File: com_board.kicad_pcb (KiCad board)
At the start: 2 copper layers, 25 parts, among them J1 USB_C_Receptacle_USB2.0_16P, J2 Conn_ST_STDC14, U1 nRF52820-QDxx, Y1 32.768kHz Cl=9pF, Y2 32MHz Cl=8pF

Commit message: Fixed libs
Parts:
- added C16: 820pF, Capacitor_SMD:C_0201_0603Metric, F.Cu at (170.0, 113.4)
- added C17: 1uF, Capacitor_SMD:C_0402_1005Metric_Pad0.74x0.62mm_HandSolder, F.Cu at (181.1, 91.5)
- added C18: 1uF, Capacitor_SMD:C_0402_1005Metric_Pad0.74x0.62mm_HandSolder, F.Cu at (181.1, 93.5)
- added H1: MountingHole, MountingHole:MountingHole_2.2mm_M2, F.Cu at (166.9, 78.2)
- added H2: MountingHole, MountingHole:MountingHole_2.2mm_M2, F.Cu at (166.9, 84.2)
- added H3: MountingHole, MountingHole:MountingHole_2.2mm_M2, F.Cu at (166.9, 90.2)
- added H4: MountingHole, MountingHole:MountingHole_2.2mm_M2, F.Cu at (166.9, 96.1)
- added IC1: nRF52820-QDAA-R, NRF52qdaa:QFN40P500X500X90-41N-D, F.Cu at (158.8, 108.0)
- added JP1: SolderJumper_3_Open, Jumper:SolderJumper-3_P1.3mm_Open_Pad1.0x1.5mm_NumberLabels, F.Cu at (158.0, 113.3)
- added POW_5V1: FFC-FPC:TE_84952_4, Connector_FFC-FPC:TE_84952-4_1x04-1MP_P1.0mm_Horizontal, F.Cu at (206.1, 93.8)
- added R1: 5.1K, Resistor_SMD:R_0402_1005Metric_Pad0.72x0.64mm_HandSolder, F.Cu at (177.2, 110.1)
- added R2: 5.1K, Resistor_SMD:R_0402_1005Metric_Pad0.72x0.64mm_HandSolder, F.Cu at (177.2, 112.0)
- added R3: 5.1K, Resistor_SMD:R_0402_1005Metric_Pad0.72x0.64mm_HandSolder, F.Cu at (177.2, 114.0)
- added TP10: TestPoint, TestPoint:TestPoint_Pad_D1.0mm, F.Cu at (150.6, 105.8)
- added TP11: TestPoint, TestPoint:TestPoint_Pad_D1.0mm, F.Cu at (150.6, 108.9)
- added TP12: TestPoint, TestPoint:TestPoint_Pad_D1.0mm, F.Cu at (150.6, 112.0)
- added TP13: TestPoint, TestPoint:TestPoint_Pad_D1.0mm, F.Cu at (153.6, 105.8)
- added TP14: TestPoint, TestPoint:TestPoint_Pad_D1.0mm, F.Cu at (153.6, 108.9)
- added TP15: TestPoint, TestPoint:TestPoint_Pad_D1.0mm, F.Cu at (153.6, 112.0)
- added TP4: TestPoint, TestPoint:TestPoint_Pad_D1.0mm, F.Cu at (144.5, 105.8)
- added TP5: TestPoint, TestPoint:TestPoint_Pad_D1.0mm, F.Cu at (144.5, 108.9)
- added TP6: TestPoint, TestPoint:TestPoint_Pad_D1.0mm, F.Cu at (144.5, 112.0)
- added TP7: TestPoint, TestPoint:TestPoint_Pad_D1.0mm, F.Cu at (147.5, 105.8)
- added TP8: TestPoint, TestPoint:TestPoint_Pad_D1.0mm, F.Cu at (147.5, 108.9)
- added TP9: TestPoint, TestPoint:TestPoint_Pad_D1.0mm, F.Cu at (147.5, 112.0)
- added U2: USBLC6-2SC6, Package_TO_SOT_SMD:SOT-23-6, F.Cu at (180.9, 101.5)
- added U5: AP2112K-3.3, Package_TO_SOT_SMD:SOT-23-5, F.Cu at (180.9, 106.1)
- U1: value nRF52820-QDxx -> BU-01; footprint Package_DFN_QFN:QFN-40-1EP_5x5mm_P0.4mm_EP3.6x3.6mm -> bu-01:BU-01
- moved J1 73.9 mm to (119.7, 117.3)
- moved C12 37.4 mm to (181.1, 89.6)
- moved C8 37.4 mm to (181.1, 87.6)
- moved TP2 30.8 mm to (141.4, 108.9)
- moved TP1 30.8 mm to (141.4, 105.8)
- moved TP3 30.8 mm to (141.4, 112.0)
- moved Y2 29.6 mm to (180.8, 110.9)
- moved Y1 28.7 mm to (181.1, 114.1)
- moved C10 25.0 mm to (173.4, 112.8)
- moved C13 25.0 mm to (173.4, 115.3)
- moved C9 25.0 mm to (173.4, 110.3)
- moved U1 21.7 mm to (145.4, 90.8)
- moved C11 21.4 mm to (167.6, 115.2)
- moved C6 21.4 mm to (167.6, 111.7)
- moved C7 21.4 mm to (167.6, 113.4)
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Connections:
- C1 pad 1: Net-(U1-XL1/P0.00) -> Net-(IC1-P0.00)
- C11 pad 1: Net-(U1-DEC3) -> Net-(IC1-DEC3)
- C12 pad 1: Net-(U1-DEC4) -> Net-(IC1-DEC4)
- C13 pad 1: Net-(U1-DECUSB) -> Net-(IC1-DECUSB)
- C14 pad 1: Net-(U1-ANT) -> Net-(IC1-ANT)
- C2 pad 1: Net-(U1-XL2/P0.01) -> Net-(IC1-P0.01)
- C3 pad 1: Net-(U1-XC1) -> Net-(IC1-XC2)
- C4 pad 1: Net-(U1-XC2) -> Net-(IC1-XC1)
- C5 pad 1: VDD_NRF -> 3.3V_VDD
- C6 pad 1: VDD_NRF -> 3.3V_VDD
- C7 pad 1: Net-(U1-DEC1) -> Net-(IC1-DEC1)
- C8 pad 1: VDD_NRF -> 3.3V_VDD
- C9 pad 1: VDD_NRF -> 3.3V_VDD
- J1 pad A1: Net-(J1-GND-PadA1) -> GND
- J1 pad A12: Net-(J1-GND-PadA1) -> GND
- J1 pad A4: Net-(J1-VBUS-PadA4) -> VBUS
- J1 pad A5: unconnected-(J1-CC1-PadA5) -> Net-(J1-CC1)
- J1 pad A6: unconnected-(J1-D+-PadA6) -> Net-(J1-D+-PadA6)
- J1 pad A7: unconnected-(J1-D--PadA7) -> Net-(J1-D--PadA7)
- J1 pad A9: Net-(J1-VBUS-PadA4) -> VBUS
- J1 pad B1: Net-(J1-GND-PadA1) -> GND
- J1 pad B12: Net-(J1-GND-PadA1) -> GND
- J1 pad B4: Net-(J1-VBUS-PadA4) -> VBUS
- J1 pad B5: unconnected-(J1-CC2-PadB5) -> Net-(J1-CC2)
- J1 pad B6: unconnected-(J1-D+-PadB6) -> Net-(J1-D+-PadA6)
- J1 pad B7: unconnected-(J1-D--PadB7) -> Net-(J1-D--PadA7)
- J1 pad B9: Net-(J1-VBUS-PadA4) -> VBUS
- J1 pad S1: unconnected-(J1-SHIELD-PadS1) -> GND
- J2 pad 3: VDD_NRF -> 3.3V_VDD
- L1 pad 1: Net-(U1-ANT) -> Net-(IC1-ANT)
- L2 pad 2: unconnected-(L2-Pad2) -> Net-(J3-SIG)
- U1 pad 1: Net-(U1-DEC1) -> unconnected-(U1-EXTON-Pad1)
- U1 pad 10: VBUS -> unconnected-(U1-GPIO5-Pad10)
- U1 pad 11: Net-(U1-DECUSB) -> unconnected-(U1-GPIO4-Pad11)
- U1 pad 16: /nRST -> GND
- U1 pad 17: unconnected-(U1-P0.20-Pad17) -> /SPI_CS
- U1 pad 18: VDD_NRF -> /SPI_MOSI
- U1 pad 19: /SWDIO -> /SPI_MISO
- U1 pad 2: Net-(U1-XL1/P0.00) -> unconnected-(U1-WAKEUP-Pad2)
- U1 pad 20: /SWDCLK -> /SPI_CLK
- U1 pad 21: unconnected-(U1-DEC5-Pad21) -> GND
- U1 pad 22: unconnected-(U1-P0.16-Pad22) -> /BU-01_IRQ
- U1 pad 23: unconnected-(U1-P0.17-Pad23) -> GND
- U1 pad 24: Net-(U1-ANT) -> GND
- U1 pad 3: Net-(U1-XL2/P0.01) -> /BU-01_RSTn
- U1 pad 5: unconnected-(U1-AIN3/P0.05-Pad5) -> 3.3V_VDD
- U1 pad 6: unconnected-(U1-P0.06-Pad6) -> 3.3V_VDD
- U1 pad 7: unconnected-(U1-P0.07-Pad7) -> 3.3V_VDD
- U1 pad 8: VDD_NRF -> GND
- U1 pad 9: VDD_NRF -> unconnected-(U1-GPIO6-Pad9)
- Y1 pad 1: Net-(U1-XL2/P0.01) -> Net-(IC1-P0.01)
- Y1 pad 2: Net-(U1-XL1/P0.00) -> Net-(IC1-P0.00)
- Y2 pad 1: Net-(U1-XC2) -> Net-(IC1-XC1)
- Y2 pad 3: Net-(U1-XC1) -> Net-(IC1-XC2)

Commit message: Almost done
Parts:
- added J3: U.FL-R-SMT_01_, UFL:HRS_U.FL-R-SMT_01_, F.Cu at (129.2, 116.1)
- moved R3 79.1 mm to (100.3, 96.0)
- moved H2 75.8 mm to (100.0, 120.0)
- moved H4 67.1 mm to (100.0, 90.0)
- moved POW_5V1 60.1 mm to (147.0, 105.0), turned to 90 degrees
- moved TP13 55.2 mm to (99.7, 94.0)
- moved C8 54.6 mm to (127.9, 99.9), turned to 90 degrees
- moved Y1 52.4 mm to (131.0, 98.9)
- moved U1 52.3 mm to (97.1, 111.0), turned to 90 degrees
- moved TP12 50.6 mm to (100.0, 113.5)
- moved C13 50.5 mm to (124.2, 104.4), turned to 180 degrees
- moved C10 50.4 mm to (124.1, 102.7), turned to 180 degrees
- moved J2 49.4 mm to (125.3, 90.5), turned to -90 degrees
- moved TP10 49.0 mm to (102.7, 95.5)
- moved C12 48.8 mm to (134.8, 105.0)
- moved C9 48.4 mm to (126.2, 99.6), turned to 90 degrees
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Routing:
- net 3.3V_VDD: track 0.00 -> 10.5 mm
- net Net-(J1-D--PadA7): track 0.00 -> 5.66 mm
- net Net-(IC1-XC1): track 0.00 -> 5.31 mm
- net GND: track 0.00 -> 5.23 mm
- net Net-(J1-D+-PadA6): track 0.00 -> 4.89 mm
- net Net-(IC1-XC2): track 0.00 -> 4.86 mm
- net Net-(IC1-P0.01): track 0.00 -> 4.41 mm
- net Net-(IC1-P0.00): track 0.00 -> 4.33 mm
- net Net-(J1-CC1): track 0.00 -> 3.34 mm
- net VBUS: track 0.00 -> 3.26 mm
- net Net-(J1-CC2): track 0.00 -> 3.21 mm
- net Net-(IC1-DECUSB): track 0.00 -> 2.75 mm
- net Net-(IC1-ANT): track 0.00 -> 2.60 mm
- net Net-(IC1-DEC1): track 0.00 -> 2.51 mm
- net Net-(J3-SIG): track 0.00 -> 2.29 mm
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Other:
- board outline added: 58 x 38 mm

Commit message: Worked on layou
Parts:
- moved C18 0.87 mm to (143.0, 115.3), turned to 0 degrees
- moved TP2 0.58 mm to (126.6, 95.9)
- moved TP6 0.43 mm to (141.6, 105.5)
- moved TP7 0.43 mm to (141.6, 103.3)
- moved C8 0.31 mm to (127.6, 100.0)
- moved TP3 0.24 mm to (129.2, 95.9)
- moved TP1 0.23 mm to (122.8, 95.9)
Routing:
- net GND: track 5.23 -> 28.9 mm, vias 0 -> 22
- net /UART_RX: track 0.00 -> 13.1 mm
- net /UART_TX: track 0.00 -> 6.58 mm, vias 0 -> 2
- net /BU-01_IRQ: track 0.00 -> 5.95 mm
- net /SPI_CS: track 0.00 -> 5.60 mm
- net 3.3V_VDD: track 10.5 -> 6.91 mm
- net Net-(J1-D+-PadA6): track 4.89 -> 6.96 mm
- net /BU-01_RSTn: track 0.00 -> 1.71 mm, vias 0 -> 1
- added copper zone on In1.Cu, net GND
- added copper zone on In2.Cu, net GND
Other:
- copper layers 2 -> 4

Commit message: first iteration
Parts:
- removed POW_5V1: FFC-FPC:TE_84952_4, Connector_FFC-FPC:TE_84952-4_1x04-1MP_P1.0mm_Horizontal
- removed TP14, TP15: TestPoint, TestPoint:TestPoint_Pad_D1.0mm
- added TP16: TestPoint, TestPoint:TestPoint_Pad_D1.0mm, F.Cu at (137.4, 108.3)
- added TP17: TestPoint, TestPoint:TestPoint_Pad_D1.0mm, F.Cu at (138.4, 105.9)
- added UART_conn1: FFC-FPC:TE_84952_6, Connector_FFC-FPC:TE_84952-6_1x06-1MP_P1.0mm_Horizontal, F.Cu at (147.0, 104.7)
- moved C9 9.10 mm to (121.5, 107.5), turned to 180 degrees
- moved C10 3.31 mm to (126.0, 100.0), turned to 90 degrees
- moved J3 1.84 mm to (128.4, 117.7)
- moved C15 1.84 mm to (127.2, 112.0)
- moved C14 1.84 mm to (127.2, 111.2)
- moved L1 1.84 mm to (128.5, 111.6)
- moved L2 1.84 mm to (128.5, 113.5)
- moved C13 1.34 mm to (124.1, 103.1)
- moved C12 0.81 mm to (135.6, 104.9)
- moved TP6 0.76 mm to (141.7, 104.8)
- moved TP7 0.57 mm to (141.7, 102.7)
- moved TP4 0.44 mm to (141.0, 120.2)
- moved C16 0.39 mm to (125.8, 108.3)
- moved C8 0.28 mm to (127.6, 99.7)
- moved TP2 0.27 mm to (126.4, 95.7)
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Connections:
- IC1 pad 33: unconnected-(IC1-P0.30-Pad33) -> /INT
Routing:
- net /BU-01_RSTn: track 1.71 -> 42.7 mm, vias 1 -> 2
- net 3.3V_VDD: track 6.91 -> 47.3 mm, vias 0 -> 43
- net /BU-01_IRQ: track 5.95 -> 45.3 mm, vias 0 -> 2
- net /SWDCLK: track 0.00 -> 33.9 mm, vias 0 -> 2
- net /SPI_CLK: track 0.00 -> 32.9 mm, vias 0 -> 2
- net /SWDIO: track 0.00 -> 31.9 mm, vias 0 -> 2
- net /SPI_MISO: track 0.00 -> 31.2 mm, vias 0 -> 2
- net VBUS: track 3.26 -> 33.3 mm, vias 0 -> 5
- net /SPI_MOSI: track 0.00 -> 28.6 mm, vias 0 -> 2
- net /SPI_CS: track 5.60 -> 31.6 mm, vias 0 -> 2
- net GND: track 28.9 -> 53.9 mm, vias 22 -> 273
- net /nRST: track 0.00 -> 23.8 mm
- net /UBS_D-: track 0.00 -> 22.5 mm, vias 0 -> 2
- net /UBS_D+: track 0.00 -> 22.3 mm, vias 0 -> 2
- net /POWER_EN: track 0.00 -> 16.1 mm
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- added copper zone on B.Cu, net 3.3V_VDD
- added copper zone on F.Cu, net 3.3V_VDD
- added copper zone on F.Cu, net GND
- added copper zone on B.Cu, net VBUS

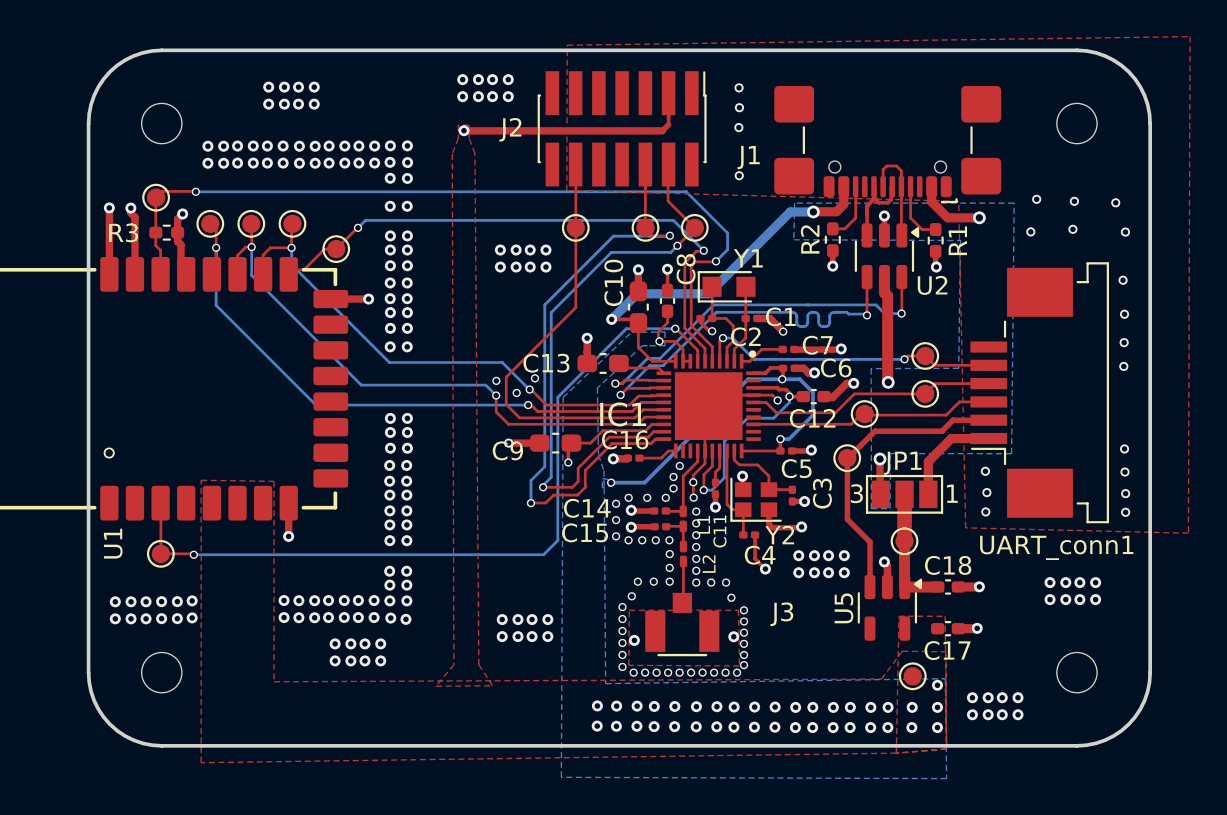
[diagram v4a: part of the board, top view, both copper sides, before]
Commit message: added name to pcb
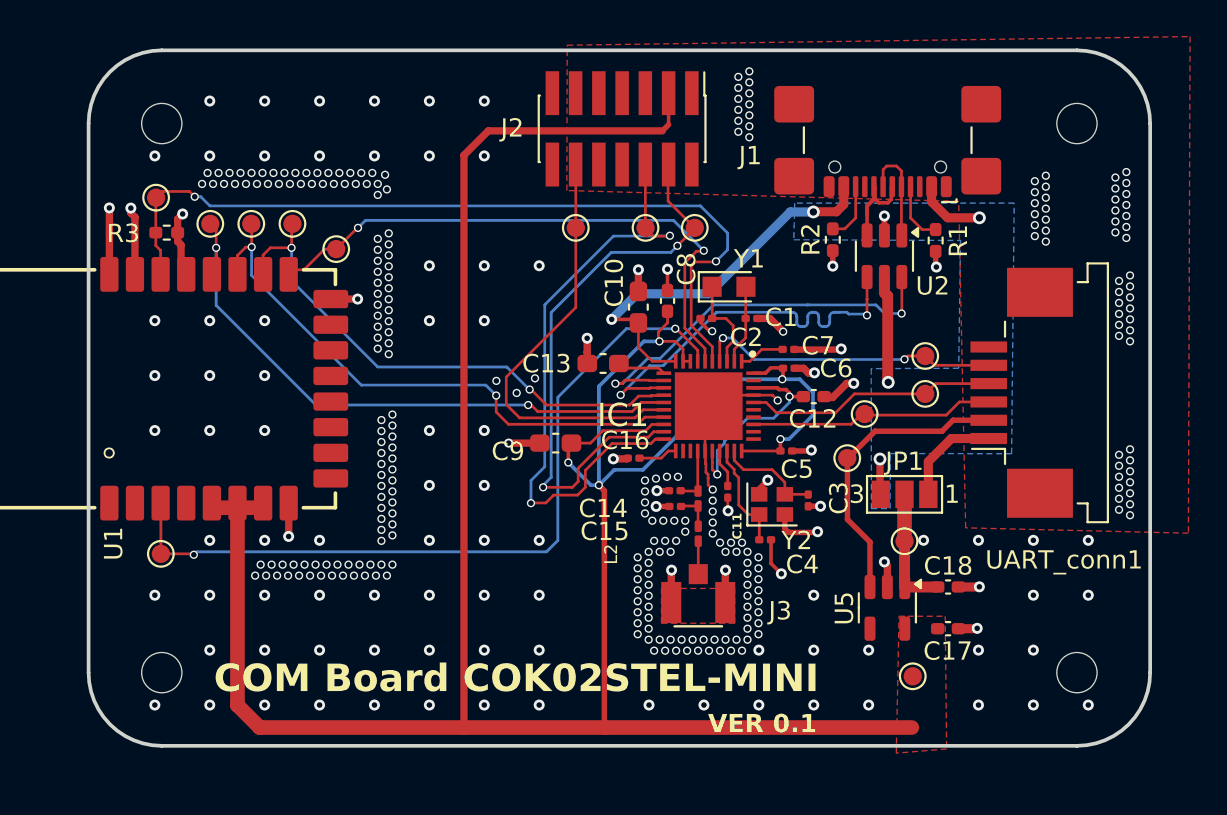
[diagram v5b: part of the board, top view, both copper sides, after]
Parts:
- moved J3 1.79 mm to (129.3, 116.2)
- moved L2 1.37 mm to (129.3, 112.4)
- moved C15 1.37 mm to (128.0, 110.9)
- moved C14 1.37 mm to (128.0, 110.1)
- moved L1 1.37 mm to (129.3, 110.5)
- moved Y2 0.91 mm to (133.3, 110.8)
- moved C3 0.91 mm to (135.3, 110.6)
- moved C4 0.91 mm to (133.0, 112.7)
- moved C11 0.69 mm to (130.9, 110.1)
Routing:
- net 3.3V_VDD: track 47.3 -> 156.4 mm, vias 43 -> 5
- net Net-(IC1-DEC4): track 13.5 -> 11.2 mm
- net Net-(IC1-ANT): track 4.56 -> 3.13 mm
- net GND: track 53.9 -> 55.2 mm, vias 273 -> 367
- net Net-(IC1-XC2): track 4.77 -> 5.70 mm
- net Net-(IC1-XC1): track 5.31 -> 5.93 mm
- net /SPI_MOSI: track 28.6 -> 29.1 mm
- removed copper zone on B.Cu, net 3.3V_VDD
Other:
- board text added: "COM Board COK02STEL-MINI"
- board text added: "VER 0.1"
- board text added: "{ "ViaStitching": "0.2", "stitch_zone_0": { "HSpacing": "3", "VSpacing": "3", "HOffset": "0", "VOffset": "0", "Clearance": "0", "Randomize": false } }"
